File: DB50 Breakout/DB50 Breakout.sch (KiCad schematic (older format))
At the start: 1 part, among them P1 CONN_02X25

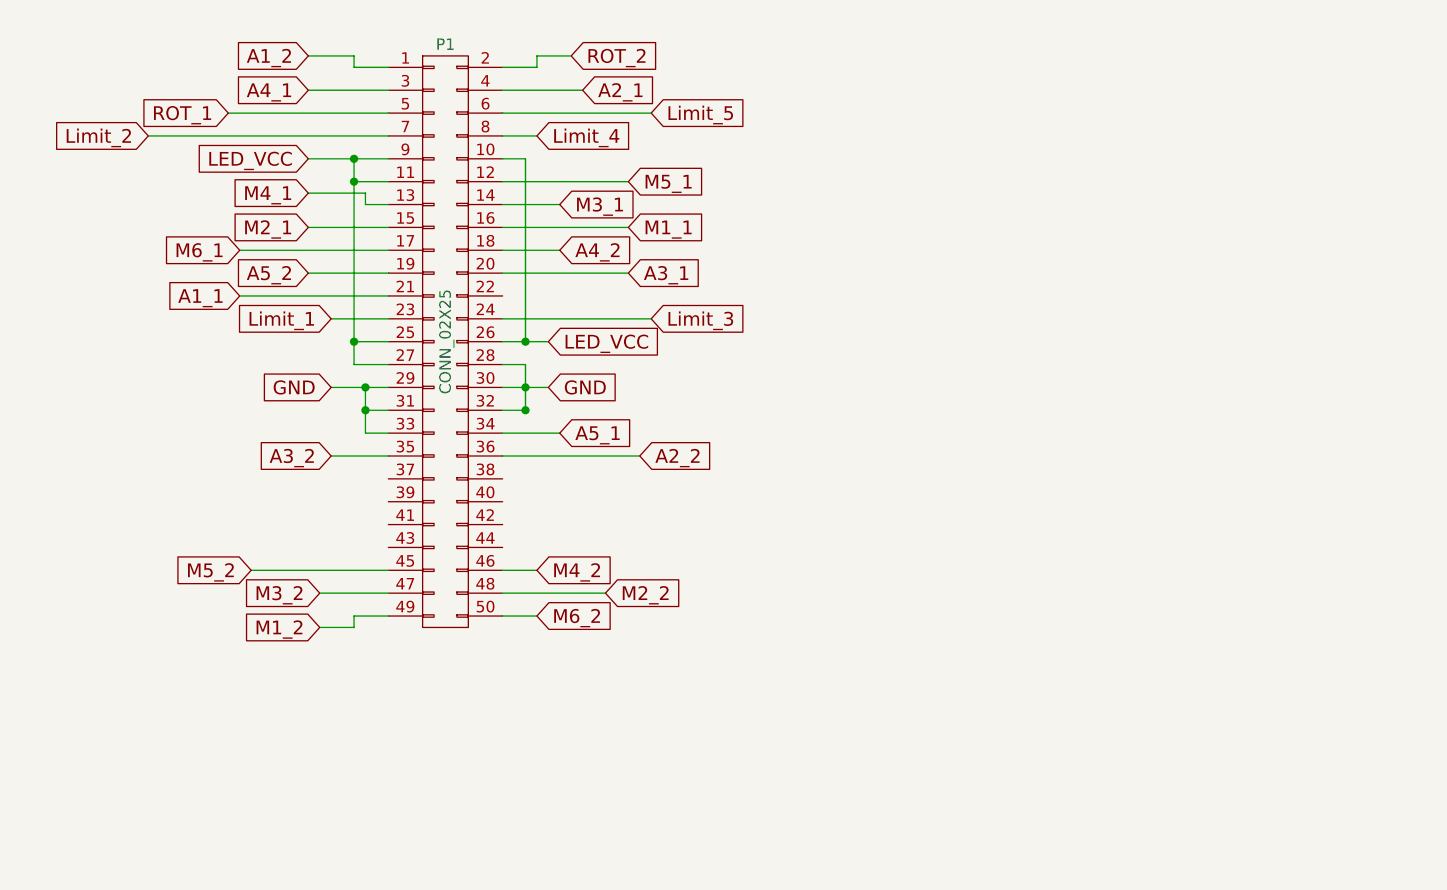
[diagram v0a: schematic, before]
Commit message: Started routing on DB50 breakout
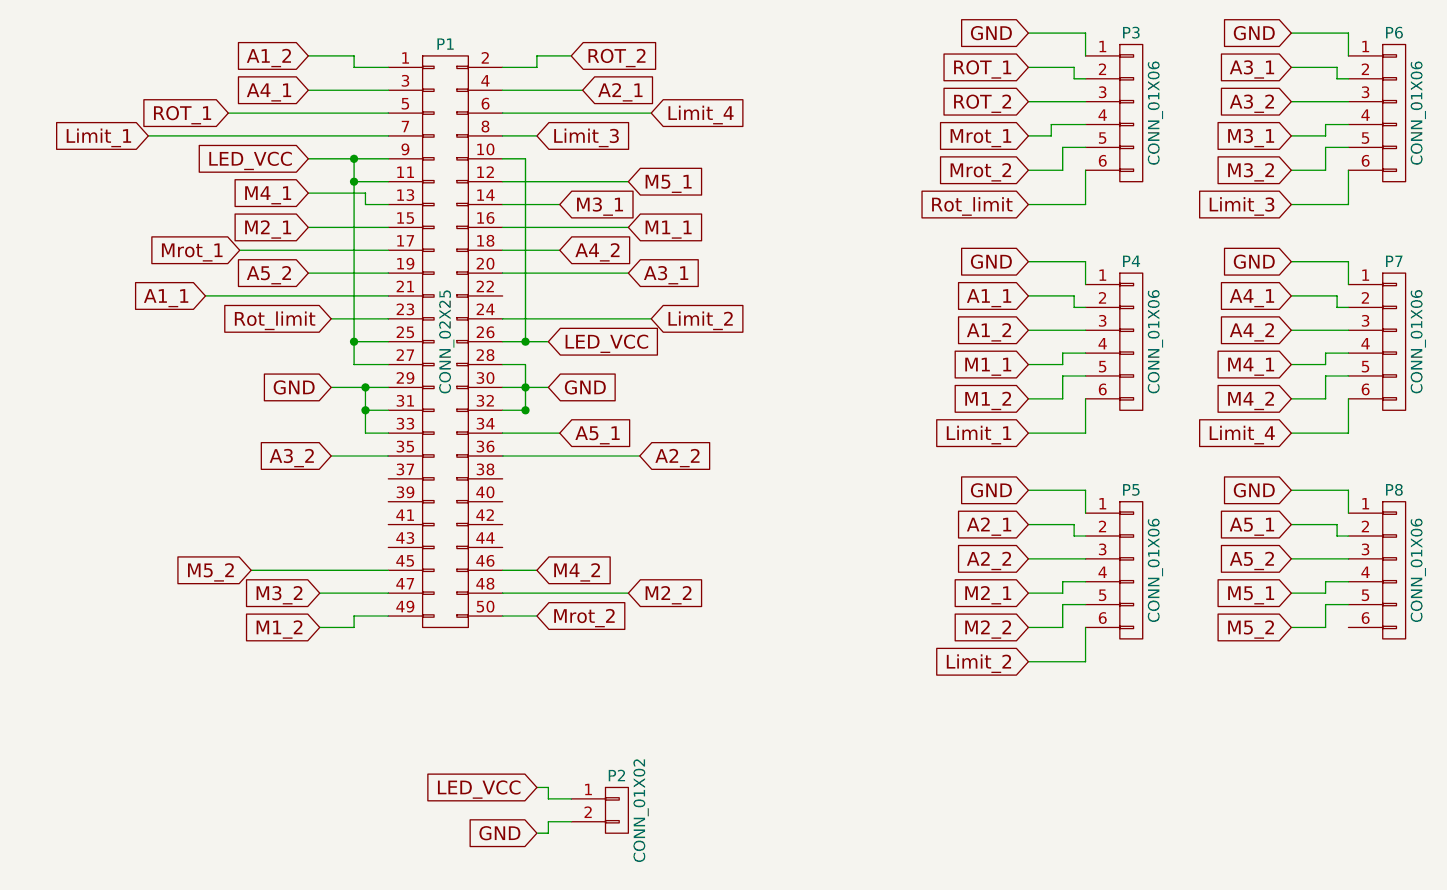
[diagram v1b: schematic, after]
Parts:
- added P2: CONN_01X02, Connector_PinHeader_2.54mm:PinHeader_1x02_P2.54mm_Vertical, symbol CONN_01X02
- added P3, P4, P5, P6, P7, P8: CONN_01X06, Connector_PinHeader_2.54mm:PinHeader_1x06_P2.54mm_Vertical, symbol CONN_01X06
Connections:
- net Limit_5 is gone; now on net Limit_4: P1.6 (P6)
- net A1_1: now also P4.2 (P2)
- net A1_2: now also P4.3 (P3)
- net A2_1: now also P5.2 (P2)
- net A2_2: now also P5.3 (P3)
- net A3_1: now also P6.2 (P2)
- net A3_2: now also P6.3 (P3)
- net A4_1: now also P7.2 (P2)
- net A4_2: now also P7.3 (P3)
- net A5_1: now also P8.2 (P2)
- net A5_2: now also P8.3 (P3)
- net GND: now also P2.2 (P2), P3.1 (P1), P4.1 (P1), P5.1 (P1), P6.1 (P1), P7.1 (P1), P8.1 (P1)
- net LED_VCC: now also P2.1 (P1)
- net Limit_1: now also P1.7 (P7), P4.6 (P6); no longer P1.23 (P23)
- net Limit_2: now also P1.24 (P24), P5.6 (P6); no longer P1.7 (P7)
- net Limit_3: now also P1.8 (P8), P6.6 (P6); no longer P1.24 (P24)
- net Limit_4: now also P7.6 (P6); no longer P1.8 (P8)
- net M1_1: now also P4.4 (P4)
- net M1_2: now also P4.5 (P5)
- net M2_1: now also P5.4 (P4)
- net M2_2: now also P5.5 (P5)
- net M3_1: now also P6.4 (P4)
- net M3_2: now also P6.5 (P5)
- net M4_1: now also P7.4 (P4)
- net M4_2: now also P7.5 (P5)
- net M5_1: now also P8.4 (P4)
- net M5_2: now also P8.5 (P5)
- net ROT_1: now also P3.2 (P2)
- net ROT_2: now also P3.3 (P3)
- net M6_1 renamed Mrot_1
- net Mrot_1: now also P3.4 (P4)
- net M6_2 renamed Mrot_2
- net Mrot_2: now also P3.5 (P5)
- new net Rot_limit: P1.23 (P23), P3.6 (P6)
